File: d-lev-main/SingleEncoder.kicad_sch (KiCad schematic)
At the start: 8 parts, among them SW2 RotaryEncoder_Switch

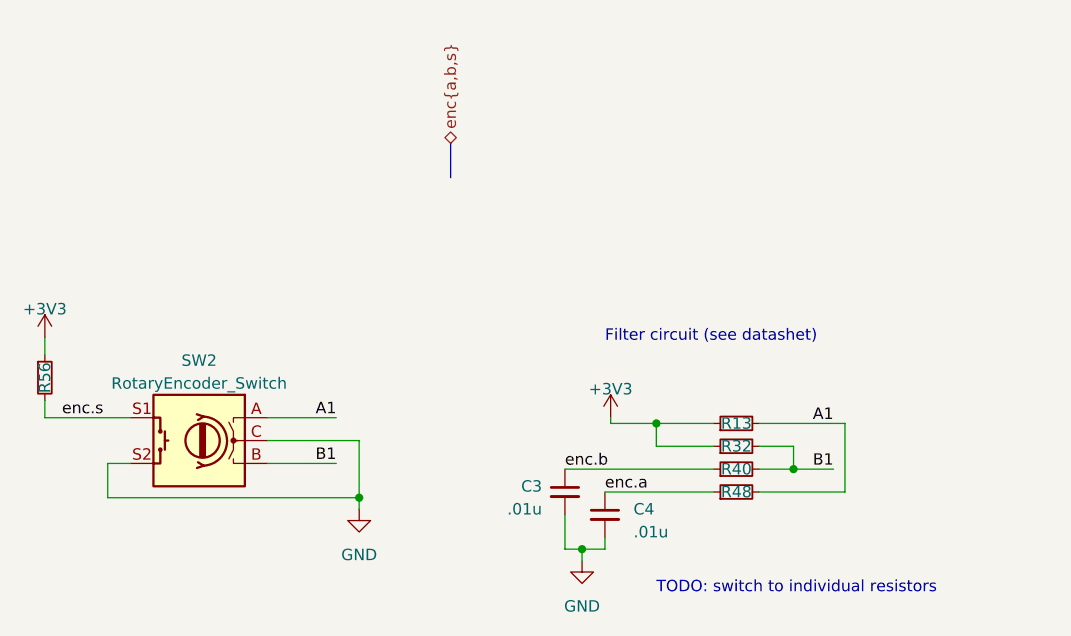
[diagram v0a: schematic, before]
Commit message: round tracks and teardrops
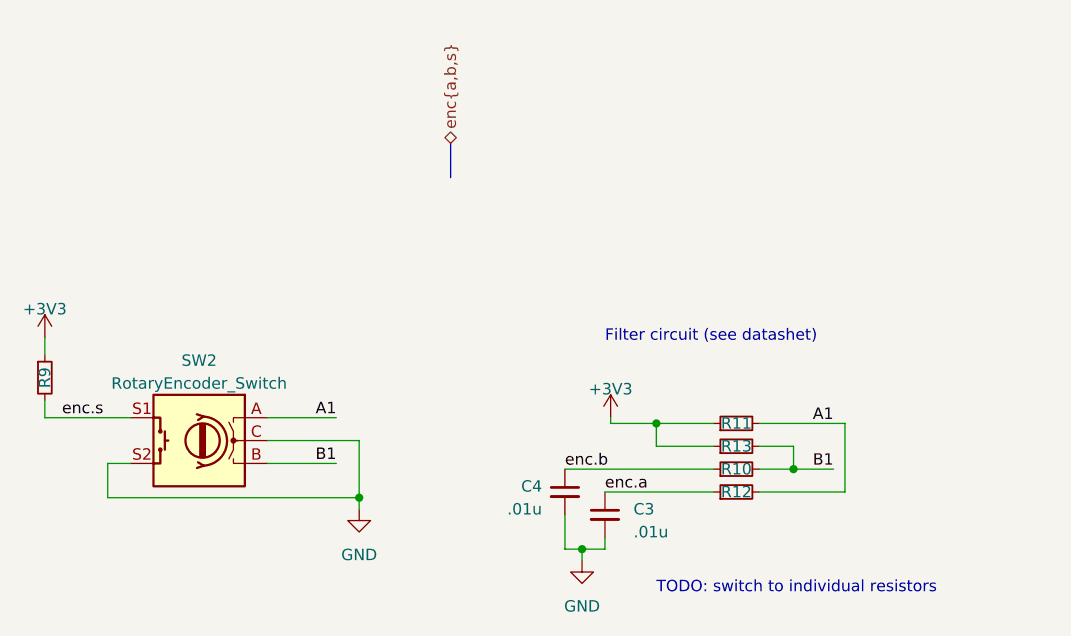
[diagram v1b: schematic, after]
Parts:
- renumbered C4 to C3, C3 to C4, R40 to R10, R13 to R11, R48 to R12, R32 to R13, R56 to R9

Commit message: Add iBOMs and additional part numbers
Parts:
- C3, C4: value .01u -> 10n; MPN (none) -> C0603C103K2RECAUTO; Notes (none) -> Common, can substitute for cheaper; Supplier (none) -> Mouser; Supplier URL (none) -> https://www.mouser.com/ProductDetail/80-C0603C103K2REAUTO
- SW2: Supplier (none) -> Aliexpress; Supplier URL (none) -> https://www.aliexpress.us/item/3256802330982050.html
